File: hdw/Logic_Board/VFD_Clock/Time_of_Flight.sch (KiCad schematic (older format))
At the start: 6 parts

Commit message: Few hdw tweaks
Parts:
- removed C?: 0.1uF, Capacitors_SMD:C_0603, symbol Custom_Library:C_Custom
- removed R?: 10k, Resistors_SMD:R_0603, symbol Custom_Library:R_Custom
- removed U?: 74LVC1G97, Package_TO_SOT_SMD:SOT-363_SC-70-6, symbol Custom_Library:74LVC1G97_Power
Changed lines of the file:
@@
 	6030 3900 5950 3900
-$Comp
-L power:GND #PWR?
-U 1 1 5B50648E
-P 3040 4200
-F 0 "#PWR?" H 3040 3950 50  0001 C CNN
-F 1 "GND" H 3040 4050 50  0000 C CNN
-F 2 "" H 3040 4200 50  0001 C CNN
-F 3 "" H 3040 4200 50  0001 C CNN
-	1    3040 4200
-	1    0    0    -1
-$EndComp
-$Comp
-L power:+3.3V #PWR?
-U 1 1 5B5064C1
-P 3040 4000
-F 0 "#PWR?" H 3040 3850 50  0001 C CNN
-F 1 "+3.3V" H 3040 4140 50  0000 C CNN
-F 2 "" H 3040 4000 50  0000 C CNN
-F 3 "" H 3040 4000 50  0000 C CNN
-	1    3040 4000
-	1    0    0    -1
-$EndComp
-$Comp
-L Custom_Library:R_Custom R?
-U 1 1 5B506A12
-P 3900 4430
-AR Path="/5A0A42E8/5B506A12" Ref="R?"  Part="1"
-AR Path="/5B4B0915/5B506A12" Ref="R?"  Part="1"
-AR Path="/5E07B870/5B506A12" Ref="R?"  Part="1"
-F 0 "R?" H 3840 4430 50  0000 R CNN
-F 1 "10k" V 3900 4430 50  0000 C CNN
-F 2 "Resistors_SMD:R_0603" H 3900 4430 50  0001 C CNN
-F 3 "" H 3900 4430 50  0001 C CNN
-F 4 "0603" H 3970 4510 50  0000 L CNN "display_footprint"
-F 5 "1%" H 3970 4430 50  0000 L CNN "Tolerance"
-F 6 "1/10W" H 3970 4360 50  0000 L CNN "Wattage"
-	1    3900 4430
-	-1   0    0    1
-$EndComp
-$Comp
-L power:GND #PWR?
-U 1 1 5B506A55
-P 3900 4580
-F 0 "#PWR?" H 3900 4330 50  0001 C CNN
-F 1 "GND" H 3900 4430 50  0000 C CNN
-F 2 "" H 3900 4580 50  0001 C CNN
-F 3 "" H 3900 4580 50  0001 C CNN
-	1    3900 4580
-	1    0    0    -1
-$EndComp
-Wire Wire Line
-	3290 4100 3900 4100
-Wire Wire Line
-	3900 4280 3900 4100
-Connection ~ 3900 4100
-Wire Wire Line
-	3900 4100 5150 4100
-Text GLabel 2740 4050 0    60   Input ~ 0
-VAN_PGOOD
-Text GLabel 2740 4150 0    60   Input ~ 0
-VFF_PGOOD
 $Comp
 L Custom_Library:C_Custom C?
@@
 $EndComp
 $Comp
-L Custom_Library:C_Custom C?
-U 1 1 5B507D27
-P 2990 4890
-F 0 "C?" H 3015 4990 50  0000 L CNN
-F 1 "0.1uF" H 3015 4790 50  0000 L CNN
-F 2 "Capacitors_SMD:C_0603" H 3028 4740 50  0001 C CNN
-F 3 "" H 3015 4990 50  0001 C CNN
-F 4 "0603" H 2840 4990 50  0000 R CNN "display_footprint"
-F 5 "50V" H 2840 4890 50  0000 R CNN "Voltage"
-F 6 "X7R" H 2840 4790 50  0000 R CNN "Dielectric"
-	1    2990 4890
-	1    0    0    -1
-$EndComp
-$Comp
-L power:+3.3V #PWR?
-U 1 1 5B507D2E
-P 2990 4740
-F 0 "#PWR?" H 2990 4590 50  0001 C CNN
-F 1 "+3.3V" H 2990 4880 50  0000 C CNN
-F 2 "" H 2990 4740 50  0000 C CNN
-F 3 "" H 2990 4740 50  0000 C CNN
-	1    2990 4740
-	1    0    0    -1
-$EndComp
-$Comp
-L power:GND #PWR?
-U 1 1 5B507D34
-P 2990 5040
-F 0 "#PWR?" H 2990 4790 50  0001 C CNN
-F 1 "GND" H 2990 4890 50  0000 C CNN
-F 2 "" H 2990 5040 50  0001 C CNN
-F 3 "" H 2990 5040 50  0001 C CNN
-	1    2990 5040
-	1    0    0    -1
-$EndComp
-$Comp
 L power:+3.3V #PWR?
 U 1 1 5B504491
@@
 I2C_SDA
 $Comp
-L Custom_Library:74LVC1G97_Power U?
-U 1 1 5E32F245
-P 3040 4100
-F 0 "U?" H 3100 4250 50  0000 L CNN
-F 1 "74LVC1G97" H 3100 3950 50  0000 L CNN
-F 2 "Package_TO_SOT_SMD:SOT-363_SC-70-6" H 3090 4100 50  0001 C CNN
-F 3 "http://www.ti.com/lit/ds/symlink/sn74lvc1g97.pdf" H 3090 4100 50  0001 C CNN
-	1    3040 4100
-	1    0    0    -1
-$EndComp
-$Comp
 L Custom_Library:I2C_Address DOC?

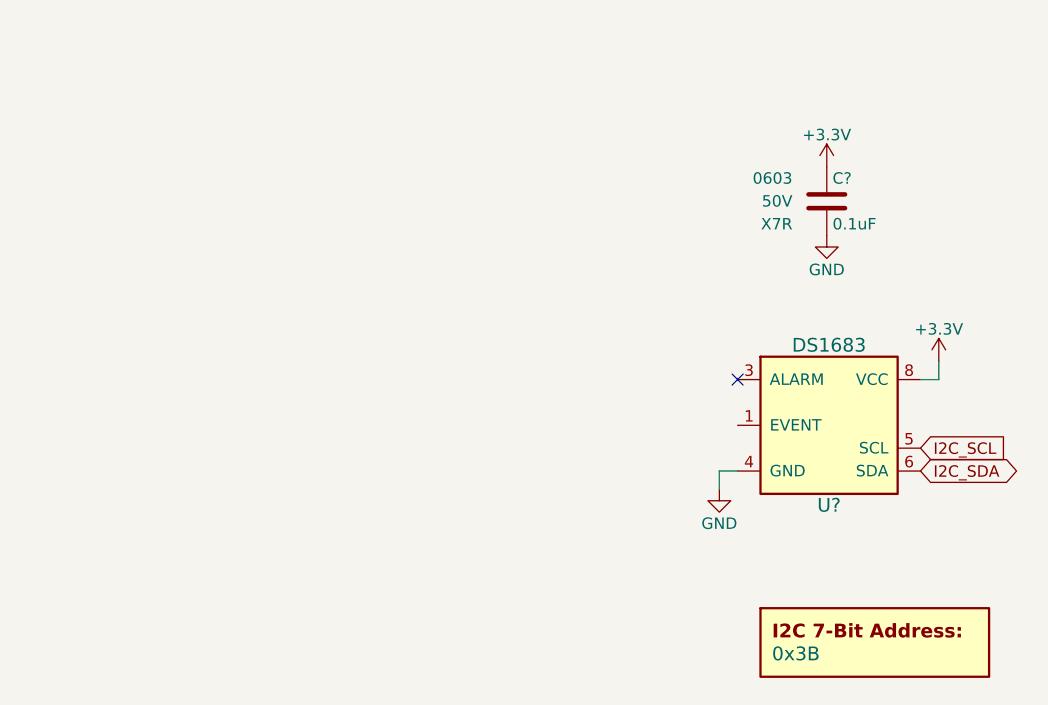
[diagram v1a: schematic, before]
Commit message: Added TOF to display board
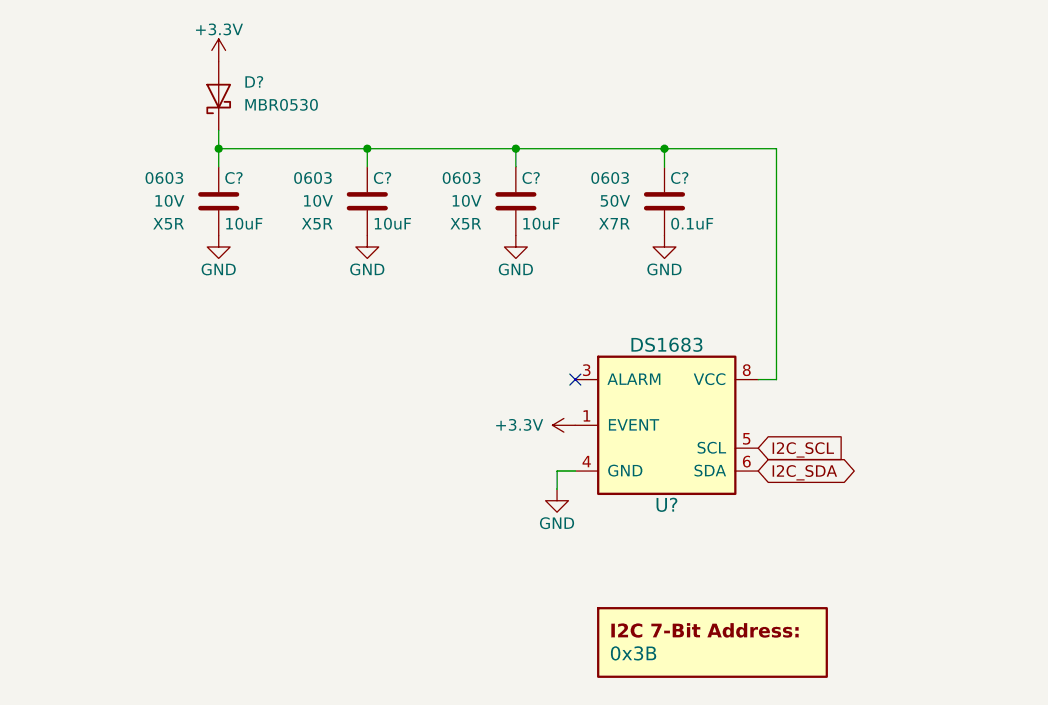
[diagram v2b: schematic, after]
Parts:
- added C? (x3): 10uF, Capacitors_SMD:C_0603, symbol Custom_Library:C_Custom
- added D?: MBR0530, Diode_SMD:D_SOD-123, symbol Diode:MBR0530
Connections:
- net +3V3: now also U?.1 (EVENT), D?.2 (A); no longer C?.1, U?.8 (VCC)
- net GND: now also C?.2, C?.2, C?.2
- new net: C?.1, C?.1, C?.1, C?.1, D?.1 (K), U?.8 (VCC)
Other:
- moved on the sheet: C?, U?

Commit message: Few fixes, added BLE
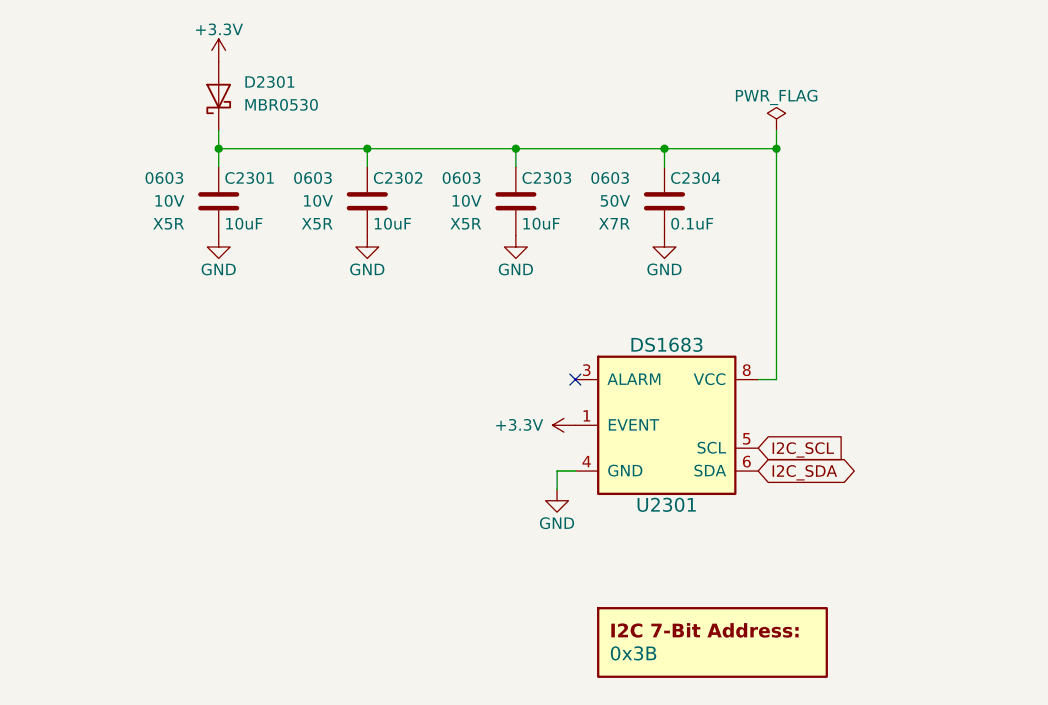
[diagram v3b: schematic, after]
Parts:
- C2304: renamed from C?; Digi-Key PN (none) -> 311-1344-1-ND
- D2301: renamed from D?; Digi-Key PN (none) -> MBR0530T1GOSCT-ND
- gave numbers to parts that had none: 5
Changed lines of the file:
@@
 $Descr A 11000 8500
 encoding utf-8
-Sheet 23 30
+Sheet 23 31
 Title ""
 Date ""
@@
 $EndDescr
 $Comp
-L Custom_Library:DS1683 U?
+L Custom_Library:DS1683 U2301
 U 1 1 5B5039F7
 P 4840 4100
-F 0 "U?" H 4840 3750 60  0000 C CNN
+F 0 "U2301" H 4840 3750 60  0000 C CNN
 F 1 "DS1683" H 4840 4450 60  0000 C CNN
 F 2 "Housings_SOIC:SOIC-8_3.9x4.9mm_Pitch1.27mm" H 4740 4400 60  0001 C CNN
@@
 NoConn ~ 4440 3900
 $Comp
-L power:GND #PWR?
+L power:GND #PWR02305
 U 1 1 5B50444E
 P 4360 4380
-F 0 "#PWR?" H 4360 4130 50  0001 C CNN
+F 0 "#PWR02305" H 4360 4130 50  0001 C CNN
 F 1 "GND" H 4360 4230 50  0000 C CNN
 F 2 "" H 4360 4380 50  0001 C CNN
@@
 	5320 3900 5240 3900
 $Comp
-L Custom_Library:C_Custom C?
+L Custom_Library:C_Custom C2304
 U 1 1 5B507AC7
 P 4830 3120
-F 0 "C?" H 4855 3220 50  0000 L CNN
+F 0 "C2304" H 4855 3220 50  0000 L CNN
 F 1 "0.1uF" H 4855 3020 50  0000 L CNN
 F 2 "Capacitors_SMD:C_0603" H 4868 2970 50  0001 C CNN
@@
 F 5 "50V" H 4680 3120 50  0000 R CNN "Voltage"
 F 6 "X7R" H 4680 3020 50  0000 R CNN "Dielectric"
+F 7 "311-1344-1-ND" H 4830 3120 50  0001 C CNN "Digi-Key PN"
 	1    4830 3120
 	1    0    0    -1
 $EndComp
 $Comp
-L power:GND #PWR?
+L power:GND #PWR02307
 U 1 1 5B507BED
 P 4830 3270
-F 0 "#PWR?" H 4830 3020 50  0001 C CNN
+F 0 "#PWR02307" H 4830 3020 50  0001 C CNN
 F 1 "GND" H 4830 3120 50  0000 C CNN
 F 2 "" H 4830 3270 50  0001 C CNN
@@
 $EndComp
 $Comp
-L Custom_Library:I2C_Address DOC?
+L Custom_Library:I2C_Address DOC2301
 U 1 1 5E383387
 P 5040 5100
-F 0 "DOC?" H 5040 5350 60  0001 C CNN
+F 0 "DOC2301" H 5040 5350 60  0001 C CNN
 F 1 "0x3B" H 4590 5100 60  0000 L CNN
 F 2 "" H 5040 5450 60  0001 C CNN
@@
 AR Path="/5E3C97B4/5E2AFB8F" Ref="C?"  Part="1"
 AR Path="/5E2A7EE3/5E2AFB8F" Ref="C?"  Part="1"
-AR Path="/5E07B870/5E2AFB8F" Ref="C?"  Part="1"
-F 0 "C?" H 4205 3220 50  0000 L CNN
+AR Path="/5E07B870/5E2AFB8F" Ref="C2303"  Part="1"
+F 0 "C2303" H 4205 3220 50  0000 L CNN
 F 1 "10uF" H 4205 3020 50  0000 L CNN
 F 2 "Capacitors_SMD:C_0603" H 4218 2970 50  0001 C CNN
@@
 AR Path="/5E3C97B4/5E2AFBB1" Ref="C?"  Part="1"
 AR Path="/5E2A7EE3/5E2AFBB1" Ref="C?"  Part="1"
-AR Path="/5E07B870/5E2AFBB1" Ref="C?"  Part="1"
-F 0 "C?" H 3555 3220 50  0000 L CNN
+AR Path="/5E07B870/5E2AFBB1" Ref="C2302"  Part="1"
+F 0 "C2302" H 3555 3220 50  0000 L CNN
 F 1 "10uF" H 3555 3020 50  0000 L CNN
 F 2 "Capacitors_SMD:C_0603" H 3568 2970 50  0001 C CNN
@@
 AR Path="/5E3C97B4/5E2B068F" Ref="C?"  Part="1"
 AR Path="/5E2A7EE3/5E2B068F" Ref="C?"  Part="1"
-AR Path="/5E07B870/5E2B068F" Ref="C?"  Part="1"
-F 0 "C?" H 2905 3220 50  0000 L CNN
+AR Path="/5E07B870/5E2B068F" Ref="C2301"  Part="1"
+F 0 "C2301" H 2905 3220 50  0000 L CNN
 F 1 "10uF" H 2905 3020 50  0000 L CNN
 F 2 "Capacitors_SMD:C_0603" H 2918 2970 50  0001 C CNN
@@
 $EndComp
 $Comp
-L power:GND #PWR?
+L power:GND #PWR02304
 U 1 1 5E2B2965
 P 4180 3270
-F 0 "#PWR?" H 4180 3020 50  0001 C CNN
+F 0 "#PWR02304" H 4180 3020 50  0001 C CNN
 F 1 "GND" H 4180 3120 50  0000 C CNN
 F 2 "" H 4180 3270 50  0001 C CNN
@@
 $EndComp
 $Comp
-L power:GND #PWR?
+L power:GND #PWR02303
 U 1 1 5E2B2CA6
 P 3530 3270
-F 0 "#PWR?" H 3530 3020 50  0001 C CNN
+F 0 "#PWR02303" H 3530 3020 50  0001 C CNN
 F 1 "GND" H 3530 3120 50  0000 C CNN
 F 2 "" H 3530 3270 50  0001 C CNN
@@
 $EndComp
 $Comp
-L power:GND #PWR?
+L power:GND #PWR02302
 U 1 1 5E2B305D
 P 2880 3270
-F 0 "#PWR?" H 2880 3020 50  0001 C CNN
+F 0 "#PWR02302" H 2880 3020 50  0001 C CNN
 F 1 "GND" H 2880 3120 50  0000 C CNN
 F 2 "" H 2880 3270 50  0001 C CNN
@@
 	4830 2890 4180 2890
 $Comp
-L Diode:MBR0530 D?
+L Diode:MBR0530 D2301
 U 1 1 5E2B5DF6
 P 2880 2660
-F 0 "D?" V 2940 2550 50  0000 R CNN
+F 0 "D2301" V 2940 2550 50  0000 R CNN
 F 1 "MBR0530" V 2840 2550 50  0000 R CNN
 F 2 "Diode_SMD:D_SOD-123" H 2880 2485 50  0001 C CNN
 F 3 "http://www.mccsemi.com/up_pdf/MBR0520~MBR0580(SOD123).pdf" H 2880 2660 50  0001 C CNN
+F 4 "MBR0530T1GOSCT-ND" H 2880 2660 50  0001 C CNN "Digi-Key PN"
 	1    2880 2660
 	0    -1   -1   0
@@
 I2C_SDA
 $Comp
-L power:+3.3V #PWR?
+L power:+3.3V #PWR02306
 U 1 1 5E36CA22
 P 4440 4100
-F 0 "#PWR?" H 4440 3950 50  0001 C CNN
+F 0 "#PWR02306" H 4440 3950 50  0001 C CNN
 F 1 "+3.3V" V 4440 4240 50  0000 L CNN
 F 2 "" H 4440 4100 50  0001 C CNN
@@
 $EndComp
 $Comp
-L power:+3.3V #PWR?
+L power:+3.3V #PWR02301
 U 1 1 5E36D120
 P 2880 2510
-F 0 "#PWR?" H 2880 2360 50  0001 C CNN
+F 0 "#PWR02301" H 2880 2360 50  0001 C CNN
 F 1 "+3.3V" H 2880 2650 50  0000 C CNN
 F 2 "" H 2880 2510 50  0001 C CNN
@@
 	1    0    0    -1
 $EndComp
+$Comp
+L power:PWR_FLAG #FLG0101
+U 1 1 5E4BADF7
+P 5320 2810
+F 0 "#FLG0101" H 5320 2885 50  0001 C CNN
+F 1 "PWR_FLAG" H 5320 2960 50  0000 C CNN
+F 2 "" H 5320 2810 50  0001 C CNN
+F 3 "~" H 5320 2810 50  0001 C CNN
+	1    5320 2810
+	1    0    0    -1
+$EndComp
+Wire Wire Line
+	5320 2810 5320 2890
+Connection ~ 5320 2890
 $EndSCHEMATC

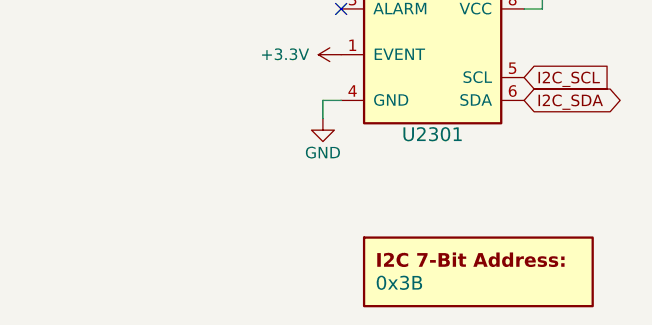
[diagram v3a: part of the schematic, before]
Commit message: Fixed I2C addresses in schematic
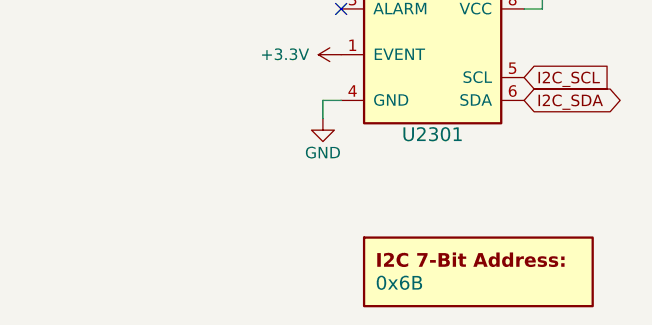
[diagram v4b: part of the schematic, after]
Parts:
- DOC2301: value 0x3B -> 0x6B
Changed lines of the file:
@@
 P 5040 5100
 F 0 "DOC2301" H 5040 5350 60  0001 C CNN
-F 1 "0x3B" H 4590 5100 60  0000 L CNN
+F 1 "0x6B" H 4590 5100 60  0000 L CNN
 F 2 "" H 5040 5450 60  0001 C CNN
 F 3 "" H 5040 5450 60  0001 C CNN
